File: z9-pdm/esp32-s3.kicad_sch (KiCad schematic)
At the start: 15 parts, among them J826 USB_C_Receptacle_USB2.0_16P, U1 TLV76733DRVx, U2201 ESP32-S3-WROOM-1

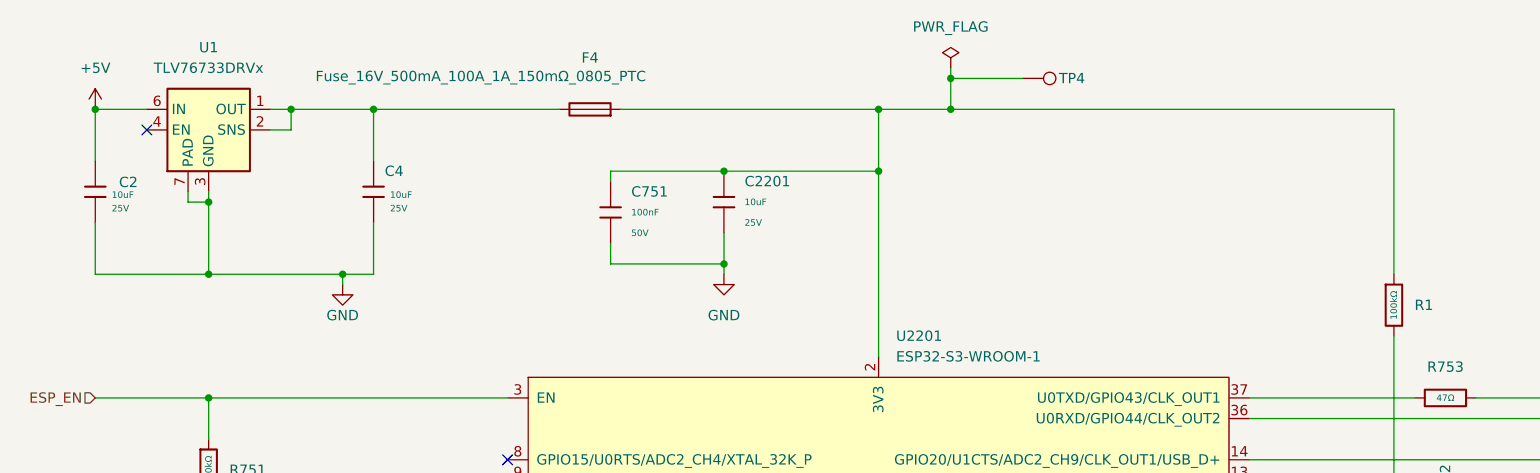
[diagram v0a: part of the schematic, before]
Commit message: new fuse and ideal diode
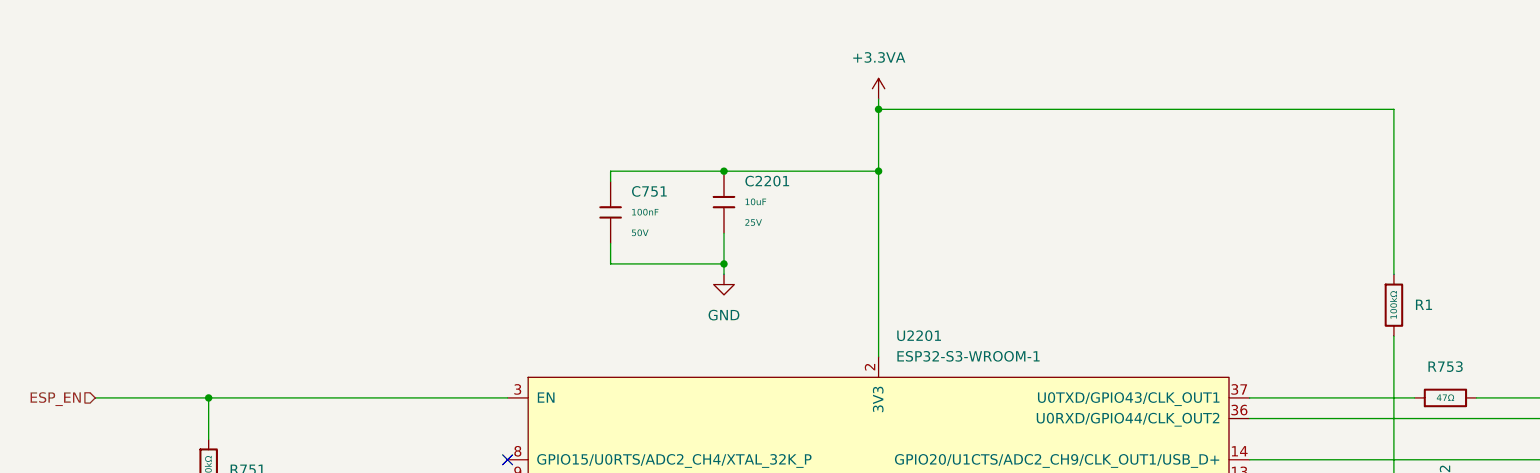
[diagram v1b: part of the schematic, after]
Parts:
- removed C2, C4: 10uF, PCM_JLCPCB:C_0603, symbol PCM_JLCPCB-Capacitors:0603,10uF,(2)
- removed F4: Fuse_16V_500mA_100A_1A_150mΩ_0805_PTC, Fuse:Fuse_0805_2012Metric, symbol dnt_global:Fuse_16V_500mA_100A_1A_150mΩ_0805_PTC_Resettable_Fuses_ROHS
- removed TP4: PE0, TestPoint:TestPoint_Pad_D1.0mm, symbol dnt_global:TestPoint_Pad_D1.0mm
- removed U1: TLV76733DRVx, Package_SON:WSON-6-1EP_2x2mm_P0.65mm_EP1x1.6mm_ThermalVias, symbol Regulator_Linear:TLV76733DRVx
- C751: symbol dnt_global:0603,100nF -> dnt_global:0603 100nF 50V X7R
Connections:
- net +3.3VA: now reaches C2201.1, C751.1, R1.1, U2201.2 (3V3)
- no-connect marks 35 -> 34

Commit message: x
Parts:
- J16: renamed from J826; footprint Connector_USB:USB_C_Receptacle_G-Switch_GT-USB-7051x -> dnt:USB_C_Receptacle_G-Switch_GT-USB-7051x
- U7: renamed from U2201; footprint PCM_Espressif:ESP32-S3-WROOM-1U -> PCM_Espressif:ESP32-S3-WROOM-1; LCSC C2980300 -> (none)
- renumbered C751 to C26, C2201 to C27, R751 to R25, R1 to R26, R753 to R27, R752 to R28, R827 to R29, R828 to R30

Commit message: passes sch drc
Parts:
- U7: value ESP32-S3-WROOM-1 -> ESP32-S3-WROOM-1U-N16R8; footprint PCM_Espressif:ESP32-S3-WROOM-1 -> PCM_Espressif:ESP32-S3-WROOM-1U; symbol PCM_Espressif:ESP32-S3-WROOM-1 -> dnt_global:ESP32-S3-WROOM-1U; LCSC (none) -> C3013946
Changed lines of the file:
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@@
 		)
 		(property "Value" "GND"
-			(at 46.99 74.9299 0)
-			(effects
-				(font
-					(size 1.27 1.27)
-				)
-				(justify left)
+			(at 44.45 78.74 0)
+			(effects
+				(font
+					(size 1.27 1.27)
+				)
 			)
 		)
@@
 		)
 		(property "Value" "GND"
-			(at 129.54 158.7499 0)
-			(effects
-				(font
-					(size 1.27 1.27)
-				)
-				(justify left)
+			(at 127 162.56 0)
+			(effects
+				(font
+					(size 1.27 1.27)
+				)
 			)
 		)
@@
 		)
 		(property "Value" "GND"
-			(at 110.49 46.9899 0)
-			(effects
-				(font
-					(size 1.27 1.27)
-				)
-				(justify left)
+			(at 107.95 50.8 0)
+			(effects
+				(font
+					(size 1.27 1.27)
+				)
 			)
 		)
@@
 		)
 		(property "Value" "+3.3VA"
-			(at 129.54 22.8599 0)
-			(effects
-				(font
-					(size 1.27 1.27)
-				)
-				(justify left)
+			(at 127 19.05 0)
+			(effects
+				(font
+					(size 1.27 1.27)
+				)
 			)
 		)
@@
 	)
 	(symbol
-		(lib_id "PCM_Espressif:ESP32-S3-WROOM-1")
+		(lib_id "dnt_global:ESP32-S3-WROOM-1U")
 		(at 127 96.52 0)
 		(unit 1)
@@
 			)
 		)
-		(property "Value" "ESP32-S3-WROOM-1"
+		(property "Value" "ESP32-S3-WROOM-1U-N16R8"
 			(at 129.1433 55.88 0)
 			(effects
@@
 			)
 		)
-		(property "Footprint" "PCM_Espressif:ESP32-S3-WROOM-1"
+		(property "Footprint" "PCM_Espressif:ESP32-S3-WROOM-1U"
 			(at 129.54 144.78 0)
 			(effects
@@
 			(at 127 96.52 0)
 			(effects
+				(font
+					(size 1.27 1.27)
+				)
+				(hide yes)
+			)
+		)
+		(property "LCSC" "C3013946"
+			(at 127 96.52 0)
+			(effects
